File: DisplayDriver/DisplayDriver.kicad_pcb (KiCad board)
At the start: 2 copper layers, 59 parts, among them J1 HTSS-108-01-G-D, J2 HEADER-1X14, SW1 (Generic) Lab Kit, U1 ESP32-S3-WROOM-1, U2 74AHCT245, U3 74AHCT245, U4 AP2112K-3.3TRG1, X1 UJ20-C-H-G-SMT-TR, X2 UJ20-C-H-G-SMT-TR

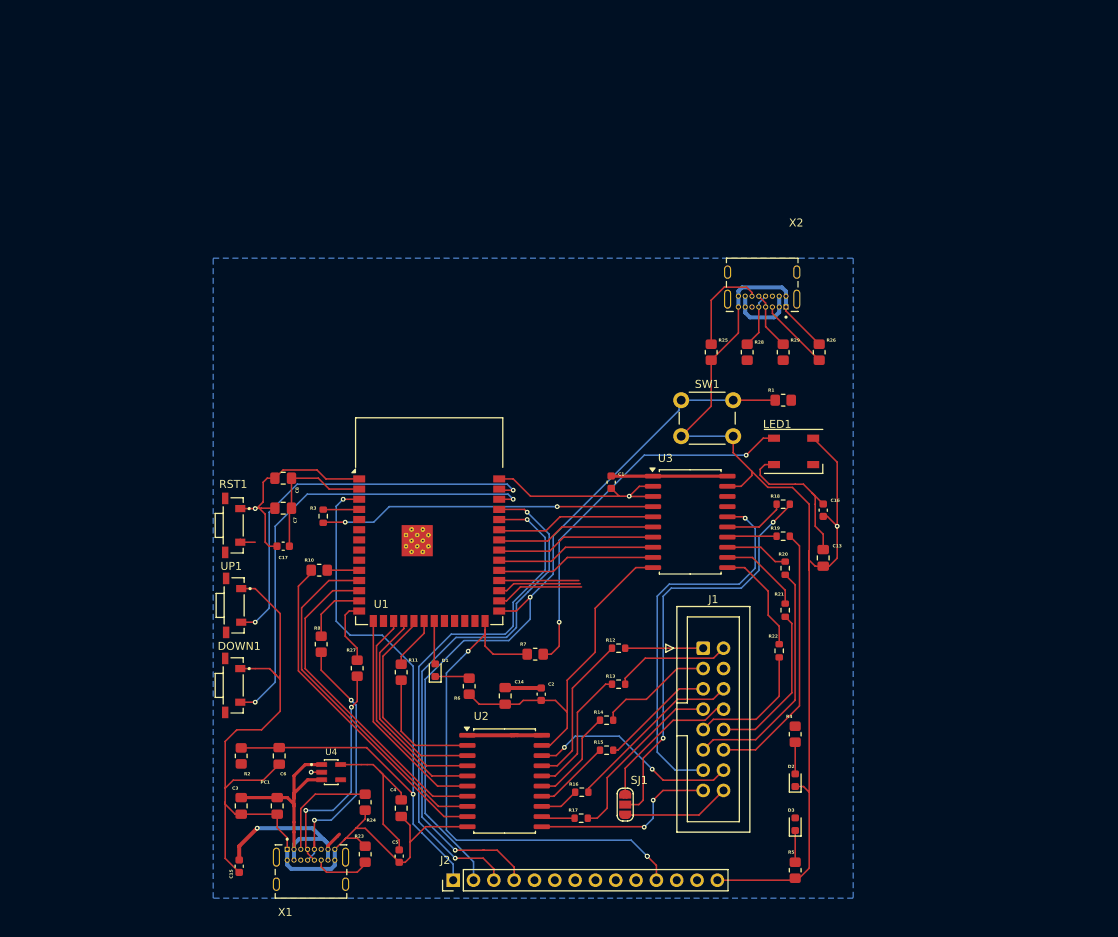
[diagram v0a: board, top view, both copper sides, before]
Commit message: PD Chip addition, proper schematic for Breadboarding today
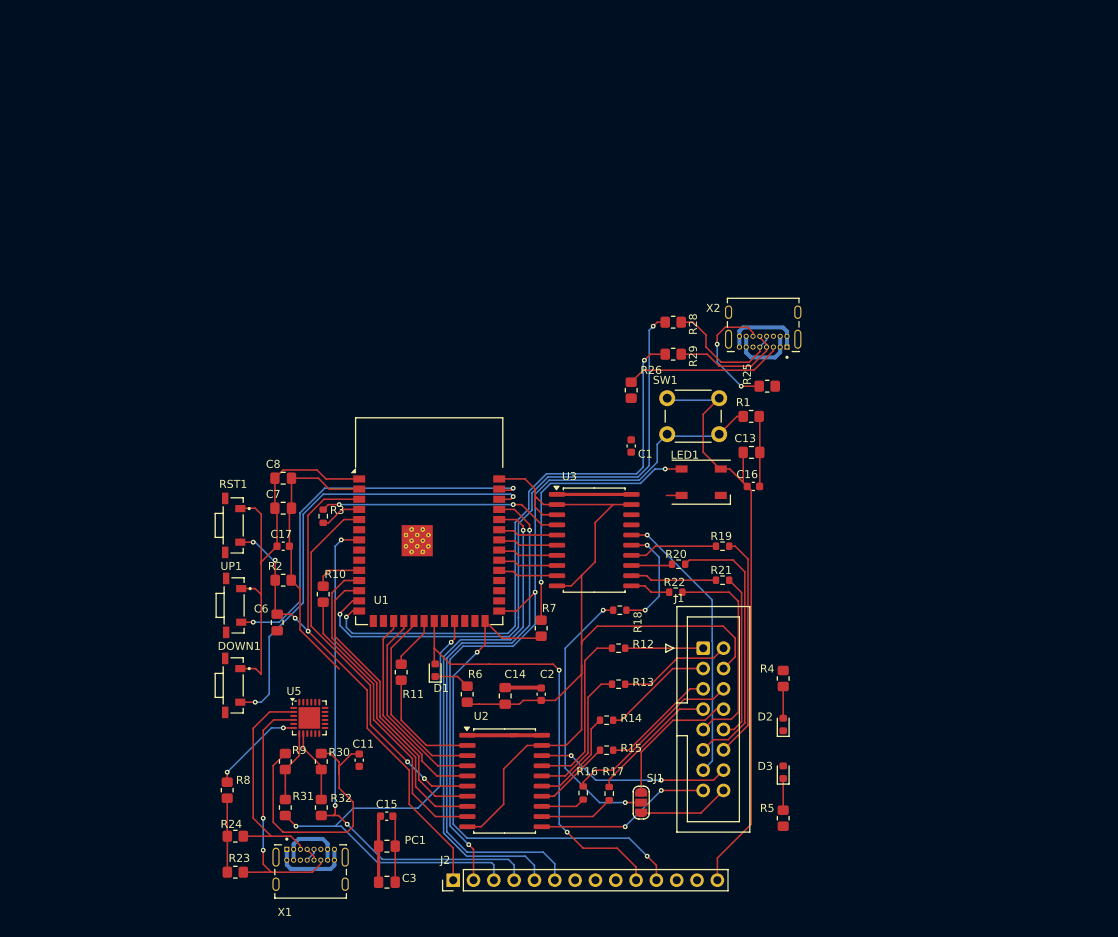
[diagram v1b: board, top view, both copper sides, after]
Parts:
- removed C4: 10uF, Capacitor_SMD:C_0805_2012Metric_Pad1.18x1.45mm_HandSolder
- removed C5: 0.1uF, Capacitor_SMD:C_0603_1608Metric
- removed R27: 22, Resistor_SMD:R_0805_2012Metric_Pad1.20x1.40mm_HandSolder
- removed U4: AP2112K-3.3TRG1, DisplayDriver:SOT95P285X140-5N
- added C11: 0.1uF, Capacitor_SMD:C_0603_1608Metric, F.Cu at (93.2, 107.8)
- added R30: 4.7k, Resistor_SMD:R_0805_2012Metric_Pad1.20x1.40mm_HandSolder, F.Cu at (88.5, 107.9)
- added R31: 22, Resistor_SMD:R_0805_2012Metric_Pad1.20x1.40mm_HandSolder, F.Cu at (84.0, 113.7)
- added R32: 22, Resistor_SMD:R_0805_2012Metric_Pad1.20x1.40mm_HandSolder, F.Cu at (88.5, 113.7)
- added R9: 4.7k, Resistor_SMD:R_0805_2012Metric_Pad1.20x1.40mm_HandSolder, F.Cu at (84.0, 107.9)
- added U5: STUSB4500QTR, Package_DFN_QFN:QFN-24-1EP_4x4mm_P0.5mm_EP2.7x2.7mm, F.Cu at (87.0, 102.5)
- J1: footprint Connector_IDC:IDC-Header_2x08_P2.54mm_Vertical -> DisplayDriver:IDC-Header_2x08_P2.54mm_Vertical
- R25, R26: value 5.1k -> 10k
- R8: value 22 -> 100k
- moved R18 24.3 mm to (125.8, 89.0), turned to 180 degrees
- moved R26 24.0 mm to (127.2, 61.5), turned to 90 degrees
- moved R2 22.6 mm to (83.8, 85.2), turned to 0 degrees
- moved R8 21.7 mm to (76.8, 111.5), turned to 90 degrees
- moved C3 20.6 mm to (96.7, 123.0), turned to 180 degrees
- moved C15 19.5 mm to (96.7, 114.8), turned to 0 degrees
- moved R24 16.8 mm to (77.8, 117.2), turned to 180 degrees
- moved C6 16.7 mm to (83.0, 90.5)
- moved R23 16.4 mm to (77.8, 121.8), turned to 180 degrees
- moved C13 15.9 mm to (142.3, 69.3), turned to 0 degrees
- moved R22 14.9 mm to (132.8, 86.8), turned to 0 degrees
- moved PC1 14.6 mm to (96.7, 118.5), turned to 0 degrees
- moved R29 13.8 mm to (132.5, 57.0), turned to 180 degrees
- moved R20 13.3 mm to (133.2, 83.2), turned to 0 degrees
- moved U3 12.2 mm to (122.6, 80.2)
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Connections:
- J2 pad 10: unconnected-(J2-Pin_10-Pad10) -> /D13
- J2 pad 3: /UART_RX -> /SCL
- J2 pad 4: /UART_TX -> /SDA
- J2 pad 5: unconnected-(J2-Pin_5-Pad5) -> /UART_RX
- J2 pad 6: unconnected-(J2-Pin_6-Pad6) -> /UART_TX
- R25 pad 2: GND -> +5V
- R26 pad 1: /CC1B -> +5V
- R26 pad 2: GND -> /CC1B
- R8 pad 1: /DN_A -> GND
- R8 pad 2: /DA- -> Net-(U5-RESET)
- U1 pad 13: /DA- -> /DB-
- U1 pad 14: /DA+ -> /DB+
- U1 pad 15: /R2_3V -> unconnected-(U1-IO3-Pad15)
- U1 pad 16: /NC8 -> unconnected-(U1-IO46-Pad16)
- U1 pad 22: /NC3 -> unconnected-(U1-IO14-Pad22)
- U1 pad 23: /NC9 -> /SCL
- U1 pad 24: /NC7 -> unconnected-(U1-IO47-Pad24)
- U1 pad 25: /NC6 -> unconnected-(U1-IO48-Pad25)
- U1 pad 5: /NC -> /R2_3V
- U1 pad 6: /NC1 -> unconnected-(U1-IO6-Pad6)
- U1 pad 7: /NC2 -> /SDA
- U1 pad 8: /NC4 -> unconnected-(U1-IO15-Pad8)
- U1 pad 9: /NC5 -> unconnected-(U1-IO16-Pad9)
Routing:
- net /DB-: track 0.00 -> 80.8 mm, vias 0 -> 2
- net /DB+: track 0.00 -> 74.4 mm, vias 0 -> 2
- net GND: track 356.6 -> 287.7 mm, vias 4 -> 0
- net /SCL: track 0.00 -> 67.1 mm, vias 0 -> 2
- net /SDA: track 0.00 -> 65.7 mm, vias 0 -> 3
- net /D13: track 5.41 -> 54.9 mm, vias 0 -> 2
- net +5V: track 79.6 -> 40.8 mm, vias 1 -> 0
- net /DN_A: track 32.5 -> 1.70 mm, vias 2 -> 0
- net /DP_A: track 28.8 -> 1.70 mm, vias 2 -> 0
- net /CC2A: track 7.29 -> 33.1 mm, vias 0 -> 2
- net 3.3V: track 58.1 -> 81.9 mm
- net /R2_3V: track 27.7 -> 47.6 mm, vias 0 -> 2
- net /M1_E: track 52.2 -> 34.2 mm
- net /CC1A: track 13.9 -> 29.1 mm
- net /CLK: track 48.9 -> 35.2 mm
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- removed copper zone on B.Cu, net GND
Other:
- board text added: "+3.3V"
- board text added: "+5V"

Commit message: Major PCB Revisions.
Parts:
- removed C11, C15: 0.1uF, Capacitor_SMD:C_0603_1608Metric
- removed C3: 10uF, Capacitor_SMD:C_0805_2012Metric_Pad1.18x1.45mm_HandSolder
- removed PC1: 100uF/6.3V, Capacitor_SMD:C_0805_2012Metric_Pad1.18x1.45mm_HandSolder
- removed R23, R24: 5.1k, Resistor_SMD:R_0805_2012Metric_Pad1.20x1.40mm_HandSolder
- removed R30, R9: 4.7k, Resistor_SMD:R_0805_2012Metric_Pad1.20x1.40mm_HandSolder
- removed R31, R32: 22, Resistor_SMD:R_0805_2012Metric_Pad1.20x1.40mm_HandSolder
- removed R8: 100k, Resistor_SMD:R_0805_2012Metric_Pad1.20x1.40mm_HandSolder
- removed U5: STUSB4500QTR, Package_DFN_QFN:QFN-24-1EP_4x4mm_P0.5mm_EP2.7x2.7mm
- removed X1: UJ20-C-H-G-SMT-TR, DisplayDriver:CUI_UJ20-C-H-G-SMT-TR
- moved X2 88.7 mm to (62.4, 87.5), turned to 0 degrees
- moved R25 79.0 mm to (67.1, 78.2), turned to 90 degrees
- moved R29 77.3 mm to (58.1, 78.1), turned to 90 degrees
- moved R5 75.8 mm to (141.9, 39.3), turned to 90 degrees
- moved R28 74.2 mm to (62.6, 78.1), turned to 90 degrees
- moved SJ1 71.1 mm to (130.1, 42.0)
- moved D3 64.4 mm to (141.9, 45.0), turned to -90 degrees
- moved R7 63.1 mm to (104.4, 29.2)
- moved D2 59.0 mm to (136.6, 45.1)
- moved R4 59.0 mm to (136.6, 39.3)
- moved C6 58.5 mm to (56.4, 38.5)
- moved R26 58.1 mm to (71.6, 78.2), turned to -90 degrees
- moved R2 52.4 mm to (60.1, 38.5), turned to -90 degrees
- moved LED1 52.1 mm to (111.6, 27.0)
- moved C16 51.0 mm to (109.1, 35.0), turned to -90 degrees
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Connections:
- J2 pad 3: /SCL -> unconnected-(J2-Pin_3-Pad3)
- J2 pad 4: /SDA -> unconnected-(J2-Pin_4-Pad4)
- U1 pad 23: /SCL -> unconnected-(U1-IO21-Pad23)
- U1 pad 38: /DOWN -> unconnected-(U1-IO2-Pad38)
- U1 pad 39: /UP -> unconnected-(U1-IO1-Pad39)
- U1 pad 7: /SDA -> unconnected-(U1-IO7-Pad7)
- U1 pad 8: unconnected-(U1-IO15-Pad8) -> /UP
- U1 pad 9: unconnected-(U1-IO16-Pad9) -> /DOWN
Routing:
- net GND: track 287.7 -> 188.5 mm, vias 0 -> 9
- net /SCL: track 67.1 -> 0.00 mm, vias 2 -> 0
- net /SDA: track 65.7 -> 0.00 mm, vias 3 -> 0
- net /DB-: track 80.8 -> 27.4 mm
- net /DB+: track 74.4 -> 29.0 mm
- net 3.3V: track 81.9 -> 43.4 mm
- net /CC2A: track 33.1 -> 0.00 mm, vias 2 -> 0
- net /M1_E16: track 11.5 -> 44.1 mm
- net /CC1A: track 29.1 -> 0.00 mm
- net Net-(LED1-DI): track 34.7 -> 7.03 mm, vias 2 -> 0
- net Net-(U3-A3): track 30.5 -> 57.4 mm
- net /UP: track 49.2 -> 22.8 mm
- net /M1_E: track 34.2 -> 7.85 mm, vias 2 -> 0
- net /DOWN: track 57.6 -> 31.9 mm
- net /NEOPIX: track 64.4 -> 85.8 mm, vias 2 -> 5
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- added copper zone on B.Cu, net GND
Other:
- board outline added: 100 x 75 mm
- board text added: "Space for +5V IN (PWR subsystem) likely: solder pads/screw connector"

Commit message: random
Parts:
- R25, R26: value 10k -> 56k
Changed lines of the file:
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@@
 		(tags "resistor")
 		(property "Reference" "R18"
-			(at -0.25 -1.25 360)
+			(at -0.25 -1.25 0)
 			(layer "F.SilkS")
 			(effects
@@
 		)
 		(fp_text user "${REFERENCE}"
-			(at 0 0 360)
+			(at 0 0 0)
 			(layer "F.Fab")
 			(effects
@@
 		)
 		(fp_text user "${REFERENCE}"
-			(at 0 0 360)
+			(at 0 0 0)
 			(layer "F.Fab")
 			(effects
@@
 		(tags "capacitor handsolder")
 		(property "Reference" "C8"
-			(at -1.25 -1.75 360)
+			(at -1.25 -1.75 0)
 			(layer "F.SilkS")
 			(effects
@@
 		)
 		(property "Value" "10uF"
-			(at 1 -1.5 360)
+			(at 1 -1.5 0)
 			(layer "F.Fab")
 			(effects
@@
 		)
 		(fp_text user "${REFERENCE}"
-			(at 0 0 360)
+			(at 0 0 0)
 			(layer "F.Fab")
 			(effects
@@
 		(tags "LED RGB NeoPixel PLCC-4 5050")
 		(property "Reference" "LED1"
-			(at -2.05 -3.4 360)
+			(at -2.05 -3.4 0)
 			(layer "F.SilkS")
 			(effects
@@
 		)
 		(property "Value" "WS2812B_3535FULL"
-			(at -0.8 3.1 360)
+			(at -0.8 3.1 0)
 			(layer "F.Fab")
 			(effects
@@
 		)
 		(fp_text user "${REFERENCE}"
-			(at 0 0 360)
+			(at 0 0 0)
 			(layer "F.Fab")
 			(effects
@@
 		(tags "LED")
 		(property "Reference" "D1"
-			(at 1 1.75 360)
+			(at 1 1.75 0)
 			(layer "F.SilkS")
 			(effects
@@
 		)
 		(property "Value" "RED"
-			(at -1.25 1.5 360)
+			(at -1.25 1.5 0)
 			(layer "F.Fab")
 			(effects
@@
 		(tags "capacitor")
 		(property "Reference" "C1"
-			(at -0.75 -1.75 360)
+			(at -0.75 -1.75 0)
 			(layer "F.SilkS")
 			(effects
@@
 		)
 		(property "Value" "0.1uF"
-			(at 1.25 -1.75 360)
+			(at 1.25 -1.75 0)
 			(layer "F.Fab")
 			(effects
@@
 		(tags "capacitor handsolder")
 		(property "Reference" "C7"
-			(at -1.25 -1.75 360)
+			(at -1.25 -1.75 0)
 			(layer "F.SilkS")
 			(effects
@@
 		)
 		(property "Value" "1uF"
-			(at 0.25 -1.5 360)
+			(at 0.25 -1.5 0)
 			(layer "F.Fab")
 			(effects
@@
 		)
 		(fp_text user "${REFERENCE}"
-			(at 0 0 360)
+			(at 0 0 0)
 			(layer "F.Fab")
 			(effects
@@
 			)
 		)
-		(property "Value" "10k"
+		(property "Value" "56k"
 			(at 0 1.65 90)
 			(layer "F.Fab")
@@
 		(tags "resistor")
 		(property "Reference" "R3"
-			(at -0.75 -2 360)
+			(at -0.75 -2 0)
 			(layer "F.SilkS")
 			(effects
@@
 		)
 		(property "Value" "33"
-			(at 0.25 -1.75 360)
+			(at 0.25 -1.75 0)
 			(layer "F.Fab")
 			(effects
@@
 			)
 		)
-		(property "Value" "10k"
+		(property "Value" "56k"
 			(at -0.25 -1.75 90)
 			(layer "F.Fab")
@@
 		(tags "capacitor")
 		(property "Reference" "C17"
-			(at 0.25 1.5 360)
+			(at 0.25 1.5 0)
 			(layer "F.SilkS")
 			(effects
@@
 		)
 		(property "Value" "0.1uF"
-			(at -2 1 360)
+			(at -2 1 0)
 			(layer "F.Fab")
 			(effects
@@
 		)
 		(fp_text user "${REFERENCE}"
-			(at 0 0 360)
+			(at 0 0 0)
 			(layer "F.Fab")
 			(effects
@@
 		)
 		(fp_text user "${REFERENCE}"
-			(at 0 0 360)
+			(at 0 0 0)
 			(layer "F.Fab")
 			(effects
@@
 		(at 62.375 87.5)
 		(property "Reference" "X2"
-			(at 6.25 0.085 360)
+			(at 6.25 0.085 0)
 			(layer "F.SilkS")
 			(effects
@@
 		)
 		(property "Value" "UJ20-C-H-G-SMT-TR"
-			(at 9 1.335 360)
+			(at 9 1.335 0)
 			(layer "F.Fab")
 			(effects
@@
 		)
 		(property "Footprint" "DisplayDriver:CUI_UJ20-C-H-G-SMT-TR"
-			(at 0 0 360)
+			(at 0 0 0)
 			(layer "F.Fab")
 			(hide yes)
@@
 		)
 		(property "Datasheet" "https://www.snapeda.com/parts/UJ20-C-H-G-SMT-TR/Same%20Sky/datasheet/"
-			(at 0 0 360)
+			(at 0 0 0)
 			(layer "F.Fab")
 			(hide yes)
@@
 		)
 		(property "Description" ""
-			(at 0 0 360)
+			(at 0 0 0)
 			(layer "F.Fab")
 			(hide yes)
@@
 		)
 		(fp_text user "PCB EDGE"
-			(at 0 1.585 360)
+			(at 0 1.585 0)
 			(layer "F.Fab")
 			(effects
@@
 	)
 	(gr_text "+3.3V"
-		(at 54.625 42.75 0)
+		(at 68.25 39.25 0)
 		(layer "User.7")
 		(effects
@@
 	)
 	(gr_text "+3.3V"
-		(at 100.625 39.5 0)
+		(at 100 40 0)
 		(layer "User.7")
 		(effects
@@
 	)
 	(gr_text "+5V"
-		(at 96.625 60.25 0)
+		(at 97 59.25 0)
 		(layer "User.8")
 		(effects
@@
 	)
 	(gr_text "+5V"
-		(at 110.375 43 0)
+		(at 107.775 43.635 0)
 		(layer "User.8")
 		(effects
@@
 	)
 	(gr_text "+5V"
-		(at 67.375 75.25 0)
+		(at 70.675 76.4 0)
 		(layer "User.8")
 		(effects

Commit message: bat footprint
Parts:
- added BT1: 1012, DisplayLibrary:BAT_1012, F.Cu at (171.0, 50.0)
- moved J1 8.84 mm to (131.0, 61.5)
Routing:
- net /CLK: track 46.8 -> 2.45 mm, vias 2 -> 1
- net /LAT: track 33.5 -> 2.06 mm
- net /M1_B2: track 23.7 -> 13.9 mm
- net /OE: track 30.0 -> 21.1 mm
- net /M1_G1: track 21.5 -> 12.7 mm
- net /M1_B1: track 19.4 -> 10.5 mm
- net /M1_R1: track 17.4 -> 8.56 mm
- net /M1_R2: track 19.8 -> 11.3 mm
- net /M1_G2: track 23.8 -> 15.8 mm
- net /M1_A: track 37.4 -> 32.4 mm
- net /M1_C: track 44.4 -> 39.5 mm
- net /M1_D: track 44.4 -> 39.7 mm
- net /M1_B: track 37.6 -> 32.9 mm
- net /M1_E8: track 35.0 -> 31.5 mm
- net /M1_E16: track 44.1 -> 40.8 mm
